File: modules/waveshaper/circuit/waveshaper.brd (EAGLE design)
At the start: 100 x 80 mm, 5 parts, among them IC2 LM324N

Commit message: Cleanup
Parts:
- removed R2: (no value), adafruit:0207/12
- added ATTENUATION, OPTOUT, POTS, POTS1, POTS2, POTS3, SIGNAL: (no value), pinhead:1X02
- added C1: 100uf, adafruit:C025-024X044
- added C2: 0.1uf, adafruit:C025-024X044
- added C3, C4: 33uf, adafruit:C025-024X044
- added JP1: (no value), pinhead:2X04
- added JP2: (no value), pinhead:1X01
- R1: value (none) -> 1K
- moved IC2 38.6 mm to (31.8, 15.2)
- moved R1 26.7 mm to (22.9, 24.1), turned to 180 degrees
- moved LM7905 10.5 mm to (7.62, 21.6)
- moved POWER 7.73 mm to (7.62, 3.81)
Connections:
- removed net 3.3V: LM7905.1, POWER.4
- removed net VDD: IC2.11, IC2.4, LM7905.2, LM7905.3, POWER.1, POWER.2, POWER.3
- new net -12V: C1.2, LM7905.2, POWER.1
- new net -5V: C2.2, IC2.11, LM7905.3
- new net 12V: POWER.2
- new net 5V: IC2.4, POWER.3
- new net GND: C1.1, C2.1, IC2.10, IC2.5, LM7905.1, POWER.4, R1.2
- new net IN: ATTENUATION.2, IC2.3, R1.1
- new net N$1: ATTENUATION.1, SIGNAL.2
- new net N$2: C3.1, IC2.6, POTS.2, POTS1.1
- new net N$3: C3.2, IC2.7, POTS1.2, POTS3.1
- new net N$4: C4.1, IC2.9, POTS2.1, POTS3.2
- new net N$5: IC2.14, OPTOUT.1
- new net N$6: IC2.13, JP1.2
- new net N$7: IC2.12, JP1.1
- new net N$8: IC2.1, IC2.2, POTS.1
- new net OUT: C4.2, IC2.8, JP2.1, POTS2.2, SIGNAL.1
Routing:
- net OUT: track 0.00 -> 67.3 mm
- net GND: track 0.00 -> 66.2 mm
- net 5V: track 0.00 -> 37.7 mm
- net N$4: track 0.00 -> 35.4 mm
- net N$5: track 0.00 -> 30.0 mm
- net -5V: track 0.00 -> 28.3 mm
- net IN: track 0.00 -> 26.6 mm
- net -12V: track 0.00 -> 25.6 mm
- net N$3: track 0.00 -> 25.5 mm
- net N$6: track 0.00 -> 24.0 mm
- net N$8: track 0.00 -> 21.6 mm
- net N$2: track 0.00 -> 21.2 mm
- net N$7: track 0.00 -> 20.4 mm
- net N$1: track 0.00 -> 2.54 mm
- net 12V: track 0.00 -> 1.27 mm
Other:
- board size 100 x 80 mm -> 55.5 x 33 mm
- board text added: "+5"
- board text added: "-12"
- board text added: "att"
- board text added: "g"
- board text added: "in"
- board text added: "nc"
- board text added: "out"
- board text added: "resistor controls"

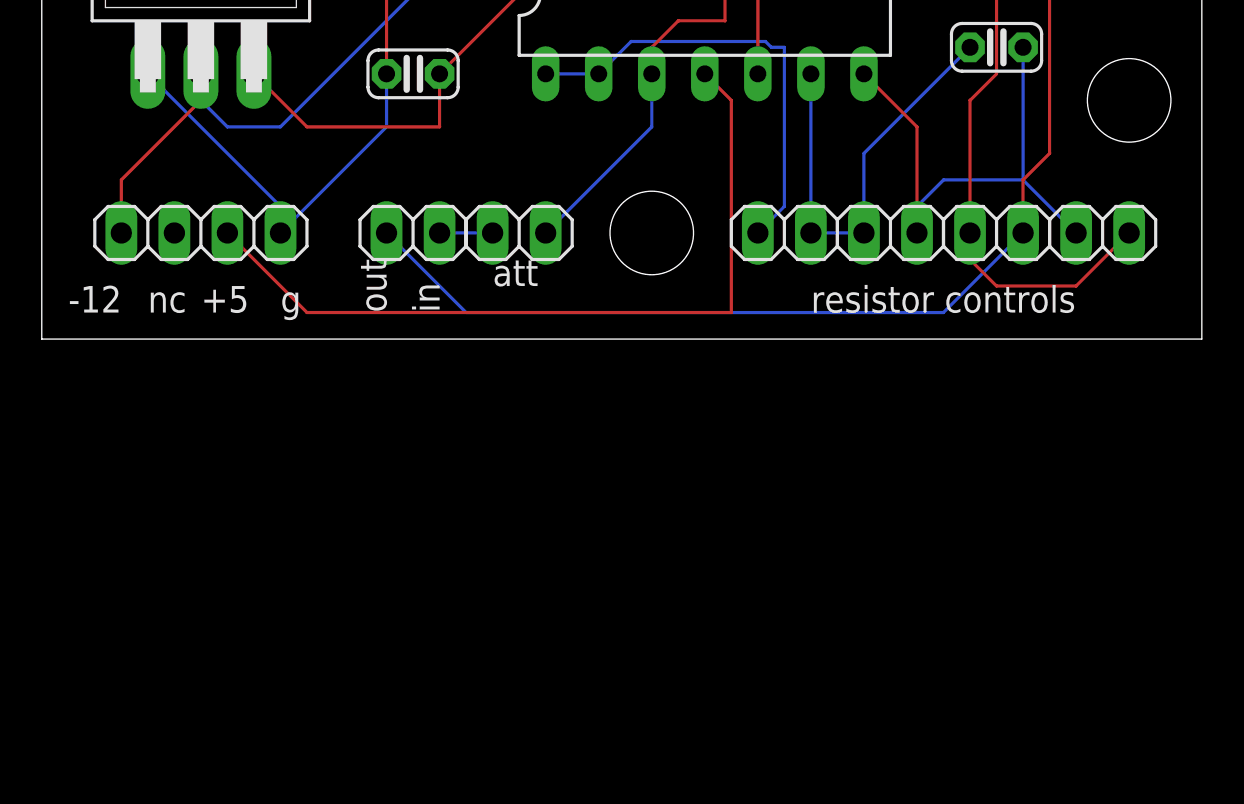
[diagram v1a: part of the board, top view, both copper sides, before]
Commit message: Adding resistors before each pots on wavshapper to avoid shorting when pot is at 0%
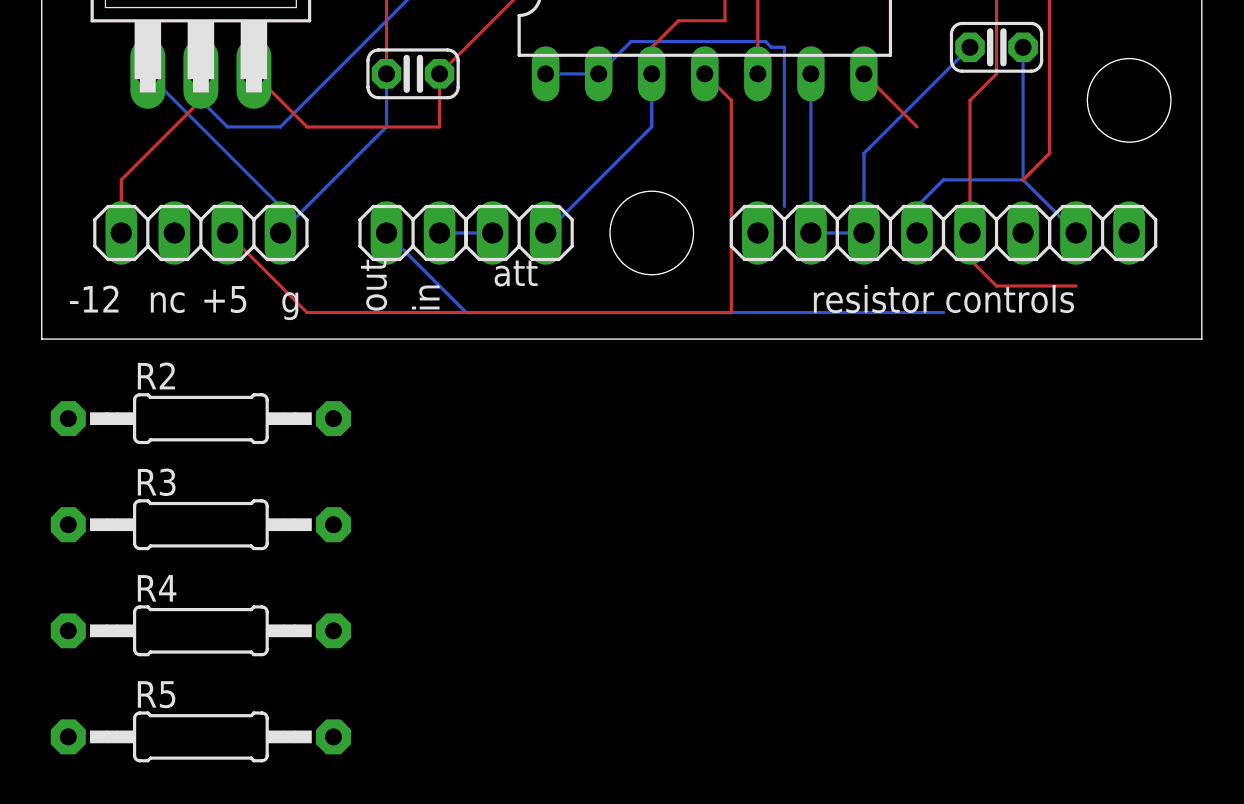
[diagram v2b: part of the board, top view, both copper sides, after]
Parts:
- added R2, R3, R4, R5: 100, adafruit:0207/12
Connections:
- new net N$10: POTS1.2, R3.1
- new net N$11: POTS2.2, R4.1
- new net N$12: POTS3.2, R5.1
- new net N$9: POTS.1, R2.1
- net N$3: now also R3.2; no longer POTS1.2
- net N$4: now also R5.2; no longer POTS3.2
- net N$8: now also R2.2; no longer POTS.1
- net OUT: now also R4.2; no longer POTS2.2
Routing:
- net OUT: track 67.3 -> 59.3 mm
- net N$3: track 25.5 -> 19.1 mm
- net N$4: track 35.4 -> 31.8 mm
- net N$8: track 21.6 -> 19.8 mm
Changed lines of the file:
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@@
 <?xml version="1.0" encoding="utf-8"?>
 <!DOCTYPE eagle SYSTEM "eagle.dtd">
-<eagle version="9.5.2">
+<eagle version="9.6.2">
 <drawing>
 <settings>
@@
 <attribute name="VALUE" x="49.53" y="23.495" size="1.27" layer="27"/>
 </element>
+<element name="R2" library="adafruit" library_urn="urn:adsk.eagle:library:420" package="0207/12" package3d_urn="urn:adsk.eagle:package:6240598/1" value="100" x="7.62" y="-5.08" smashed="yes">
+<attribute name="NAME" x="4.445" y="-3.683" size="1.27" layer="25" ratio="10"/>
+<attribute name="VALUE" x="5.334" y="-5.7658" size="1.27" layer="27" ratio="10"/>
+</element>
+<element name="R3" library="adafruit" library_urn="urn:adsk.eagle:library:420" package="0207/12" package3d_urn="urn:adsk.eagle:package:6240598/1" value="100" x="7.62" y="-10.16" smashed="yes">
+<attribute name="NAME" x="4.445" y="-8.763" size="1.27" layer="25" ratio="10"/>
+<attribute name="VALUE" x="5.334" y="-10.8458" size="1.27" layer="27" ratio="10"/>
+</element>
+<element name="R4" library="adafruit" library_urn="urn:adsk.eagle:library:420" package="0207/12" package3d_urn="urn:adsk.eagle:package:6240598/1" value="100" x="7.62" y="-15.24" smashed="yes">
+<attribute name="NAME" x="4.445" y="-13.843" size="1.27" layer="25" ratio="10"/>
+<attribute name="VALUE" x="5.334" y="-15.9258" size="1.27" layer="27" ratio="10"/>
+</element>
+<element name="R5" library="adafruit" library_urn="urn:adsk.eagle:library:420" package="0207/12" package3d_urn="urn:adsk.eagle:package:6240598/1" value="100" x="7.62" y="-20.32" smashed="yes">
+<attribute name="NAME" x="4.445" y="-18.923" size="1.27" layer="25" ratio="10"/>
+<attribute name="VALUE" x="5.334" y="-21.0058" size="1.27" layer="27" ratio="10"/>
+</element>
 </elements>
 <signals>
@@
 <contactref element="C4" pad="2"/>
 <contactref element="IC2" pad="8"/>
-<contactref element="POTS2" pad="2"/>
 <contactref element="JP2" pad="1"/>
 <wire x1="50.8" y1="26.67" x2="50.8" y2="24.13" width="0.1524" layer="1"/>
@@
 <wire x1="48.26" y1="16.51" x2="48.26" y2="7.62" width="0.1524" layer="1"/>
 <wire x1="48.26" y1="7.62" x2="46.99" y2="6.35" width="0.1524" layer="1"/>
-<wire x1="46.99" y1="6.35" x2="46.99" y2="3.81" width="0.1524" layer="1"/>
 <wire x1="39.37" y1="19.05" x2="40.64" y2="20.32" width="0.1524" layer="1"/>
 <wire x1="40.64" y1="20.32" x2="46.99" y2="20.32" width="0.1524" layer="1"/>
 <wire x1="16.51" y1="3.81" x2="20.32" y2="0" width="0.1524" layer="16"/>
 <wire x1="20.32" y1="0" x2="43.18" y2="0" width="0.1524" layer="16"/>
-<wire x1="43.18" y1="0" x2="46.99" y2="3.81" width="0.1524" layer="16"/>
+<contactref element="R4" pad="2"/>
+<wire x1="43.18" y1="0" x2="46.99" y2="6.35" width="0" layer="19" extent="1-16"/>
+<wire x1="13.97" y1="-15.24" x2="16.51" y2="3.81" width="0" layer="19" extent="1-1"/>
 </signal>
 <signal name="N$2">
@@
 <signal name="N$3">
 <contactref element="IC2" pad="7"/>
-<contactref element="POTS1" pad="2"/>
 <contactref element="C3" pad="2"/>
 <contactref element="POTS3" pad="1"/>
 <wire x1="39.37" y1="11.43" x2="41.91" y2="8.89" width="0.1524" layer="1"/>
-<wire x1="41.91" y1="8.89" x2="41.91" y2="3.81" width="0.1524" layer="1"/>
 <wire x1="49.53" y1="3.81" x2="46.99" y2="6.35" width="0.1524" layer="16"/>
 <wire x1="46.99" y1="6.35" x2="43.18" y2="6.35" width="0.1524" layer="16"/>
 <wire x1="43.18" y1="6.35" x2="41.91" y2="5.08" width="0.1524" layer="16"/>
-<wire x1="41.91" y1="5.08" x2="41.91" y2="3.81" width="0.1524" layer="16"/>
 <wire x1="46.99" y1="12.7" x2="46.99" y2="6.35" width="0.1524" layer="16"/>
+<contactref element="R3" pad="2"/>
+<wire x1="41.91" y1="5.08" x2="41.91" y2="8.89" width="0" layer="19" extent="1-16"/>
+<wire x1="13.97" y1="-10.16" x2="41.91" y2="5.08" width="0" layer="19" extent="16-16"/>
 </signal>
 <signal name="N$4">
-<contactref element="POTS3" pad="2"/>
 <contactref element="IC2" pad="9"/>
 <contactref element="C4" pad="1"/>
@@
 <wire x1="45.72" y1="11.43" x2="45.72" y2="16.51" width="0.1524" layer="1"/>
 <wire x1="45.72" y1="16.51" x2="44.45" y2="17.78" width="0.1524" layer="1"/>
-<wire x1="52.07" y1="3.81" x2="49.53" y2="1.27" width="0.1524" layer="1"/>
 <wire x1="49.53" y1="1.27" x2="45.72" y2="1.27" width="0.1524" layer="1"/>
 <wire x1="45.72" y1="1.27" x2="44.45" y2="2.54" width="0.1524" layer="1"/>
 <wire x1="44.45" y1="2.54" x2="44.45" y2="3.81" width="0.1524" layer="1"/>
+<contactref element="R5" pad="2"/>
+<wire x1="13.97" y1="-20.32" x2="44.45" y2="3.81" width="0" layer="19" extent="1-1"/>
 </signal>
 <signal name="N$5">
@@
 <contactref element="IC2" pad="2"/>
 <wire x1="24.13" y1="11.43" x2="26.67" y2="11.43" width="0.1524" layer="16"/>
-<contactref element="POTS" pad="1"/>
 <wire x1="34.6582375" y1="12.9794" x2="34.9376375" y2="12.7" width="0.1524" layer="16"/>
 <wire x1="34.9376375" y1="12.7" x2="35.56" y2="12.7" width="0.1524" layer="16"/>
@@
 <wire x1="28.2194" y1="12.9794" x2="34.6582375" y2="12.9794" width="0.1524" layer="16"/>
 <wire x1="35.56" y1="12.7" x2="35.56" y2="5.08" width="0.1524" layer="16"/>
-<wire x1="35.56" y1="5.08" x2="34.29" y2="3.81" width="0.1524" layer="16"/>
+<contactref element="R2" pad="2"/>
+<wire x1="13.97" y1="-5.08" x2="24.13" y2="11.43" width="0" layer="19" extent="1-1"/>
 </signal>
 <signal name="-12V">
@@
 <wire x1="29.21" y1="16.51" x2="26.67" y2="16.51" width="0.1524" layer="1"/>
 </signal>
+<signal name="N$9">
+<contactref element="POTS" pad="1"/>
+<contactref element="R2" pad="1"/>
+<wire x1="1.27" y1="-5.08" x2="34.29" y2="3.81" width="0" layer="19" extent="1-1"/>
+</signal>
+<signal name="N$10">
+<contactref element="POTS1" pad="2"/>
+<contactref element="R3" pad="1"/>
+<wire x1="1.27" y1="-10.16" x2="41.91" y2="3.81" width="0" layer="19" extent="1-1"/>
+</signal>
+<signal name="N$11">
+<contactref element="POTS2" pad="2"/>
+<contactref element="R4" pad="1"/>
+<wire x1="1.27" y1="-15.24" x2="46.99" y2="3.81" width="0" layer="19" extent="1-1"/>
+</signal>
+<signal name="N$12">
+<contactref element="POTS3" pad="2"/>
+<contactref element="R5" pad="1"/>
+<wire x1="1.27" y1="-20.32" x2="52.07" y2="3.81" width="0" layer="19" extent="1-1"/>
+</signal>
 </signals>
